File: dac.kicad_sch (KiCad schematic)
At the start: 53 parts, among them J9 DAC OUT, Q2 FMMT591, Q3 FMMT491, Q4 FMMT491, Q5 FMMT591, U1 CJC4334H, U9 OPA1612AxD

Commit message: Fixed VA/2
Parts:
- removed R52, R53: 10kΩ, PCM_JLCPCB:R_0805, symbol PCM_JLCPCB-Resistors:0805,10kΩ
- added R52, R53: 2.2kΩ, PCM_JLCPCB:R_0805, symbol PCM_JLCPCB-Resistors:0805,2.2kΩ
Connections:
- net GNDA: now also R52.1
- net VAO: now also R53.2
- net VA/2: now also R52.2, R53.1

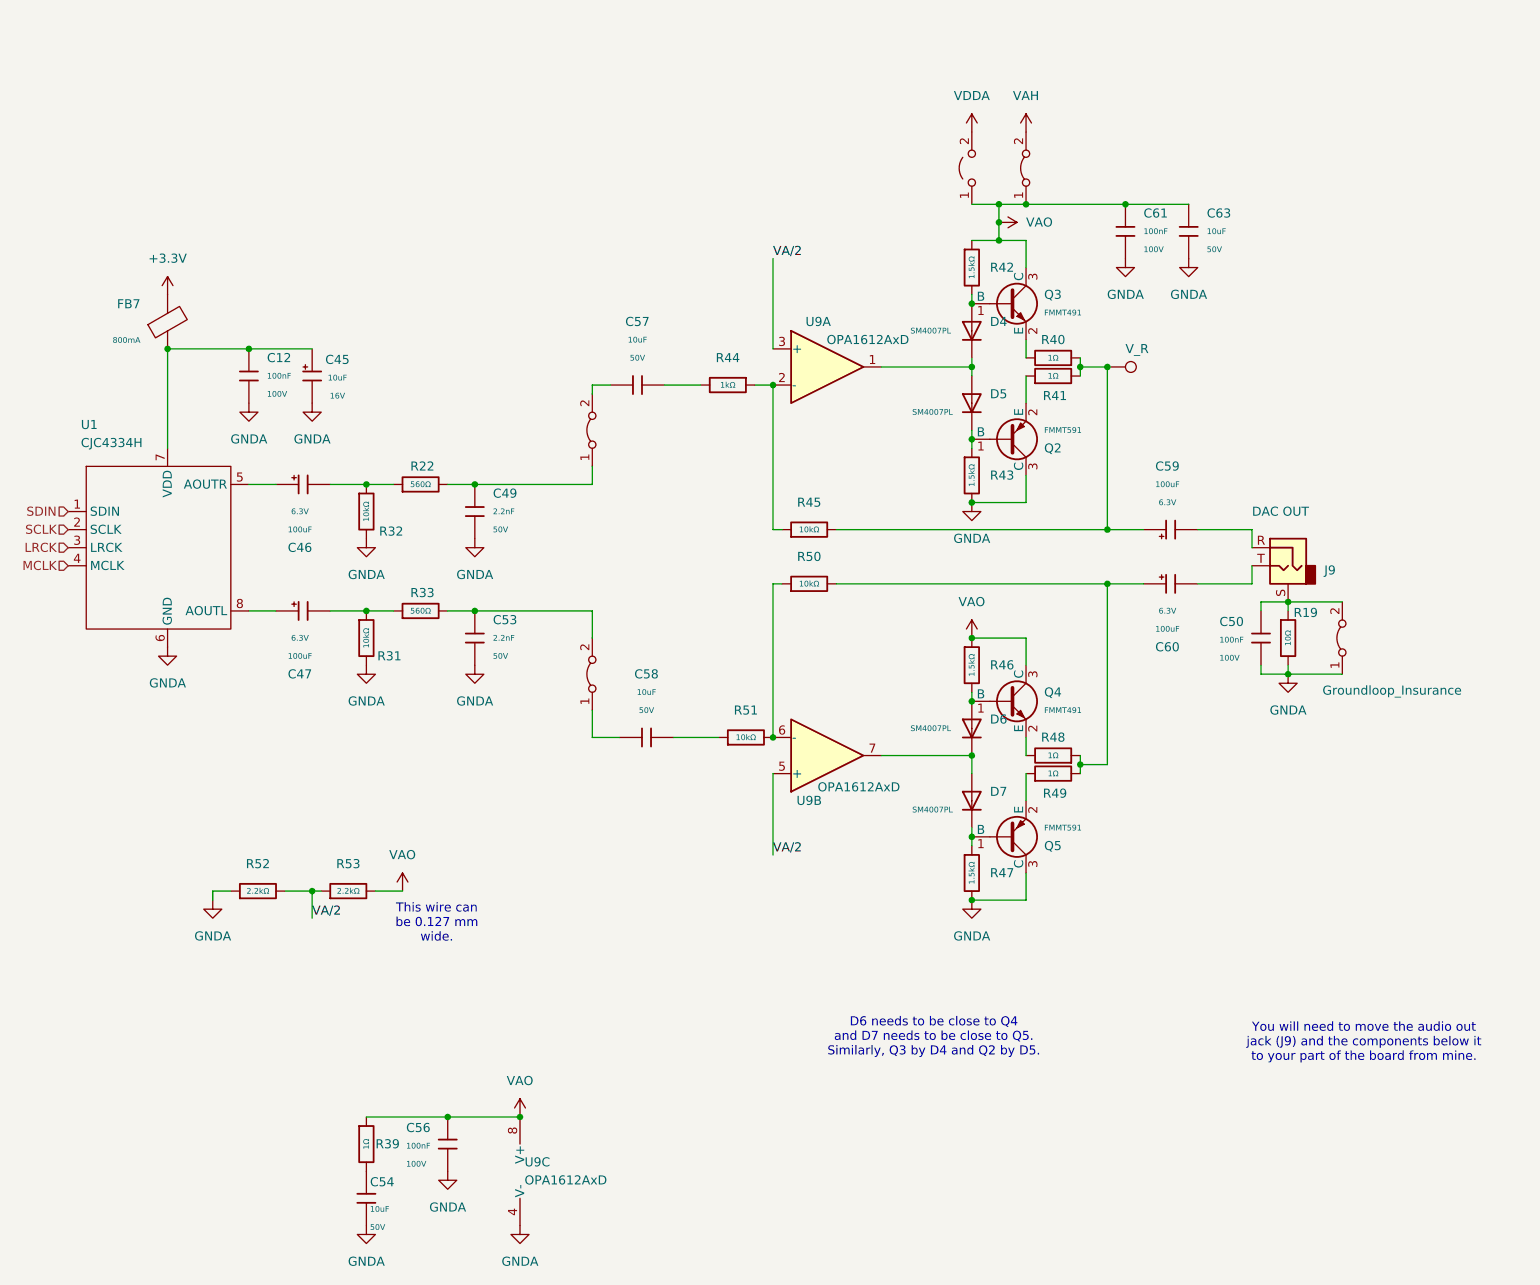
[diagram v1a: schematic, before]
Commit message: Changes from simulations.
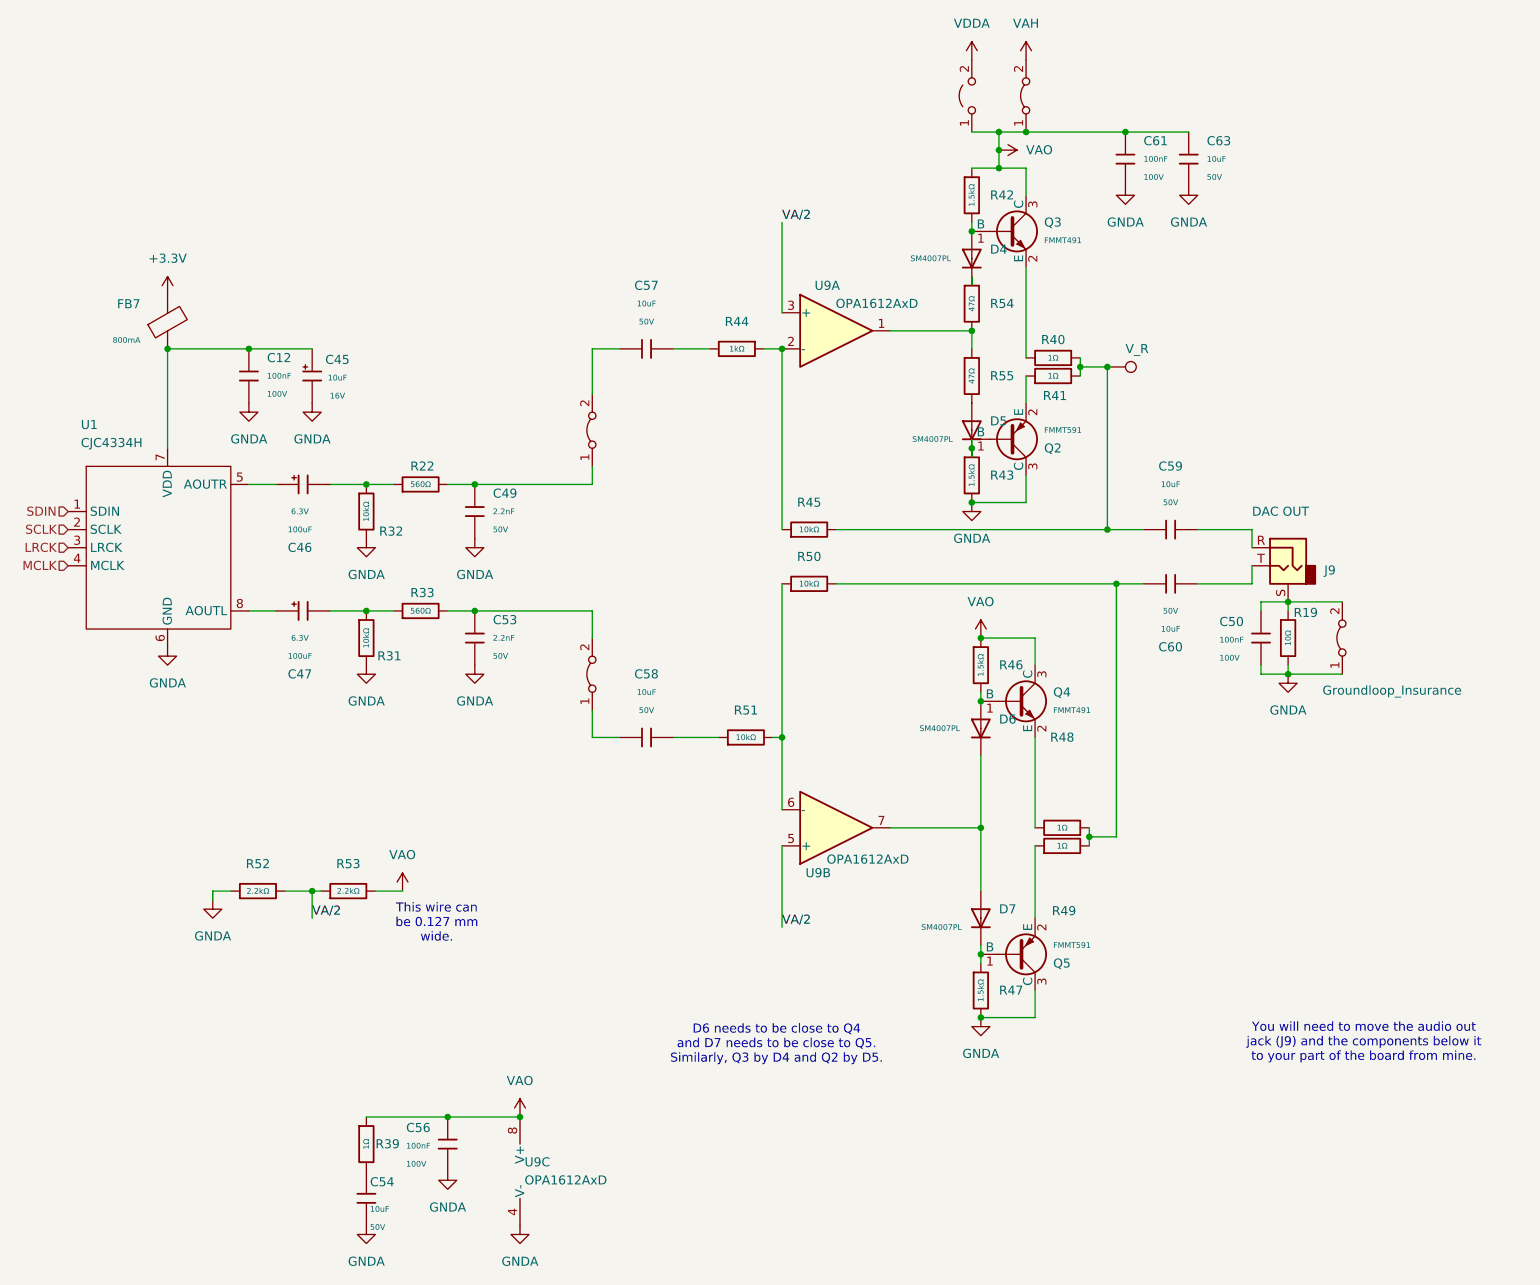
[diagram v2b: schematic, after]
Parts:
- removed C59, C60: 100uF, PCM_JLCPCB:C_CASE-B-3528-21(mm), symbol PCM_JLCPCB-Capacitors:CASE-B-3528-21(mm),100uF
- added C59, C60: 10uF, PCM_JLCPCB:C_0805, symbol PCM_JLCPCB-Capacitors:0805,10uF,(2)
- added R54, R55: 47Ω, PCM_JLCPCB:R_0805, symbol PCM_JLCPCB-Resistors:0805,47Ω
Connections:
- net at R48.1, R49.2, R50.2: now also C60.1
- net at J9.T: now also C60.2
- net at J9.R: now also C59.2
- net at R40.1, R41.2, R45.2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: now also C59.1
- new net: D4.1, R54.1
- new net: R54.2, R55.1, U9.1
- new net: D5.2, R55.2
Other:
- moved on the sheet: C57, C61, C63, D4, D5, D6, D7, Q3, Q4, Q5, R42, R44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

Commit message: Forgot the other channel.
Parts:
- removed R54, R55: 47Ω, PCM_JLCPCB:R_0805, symbol PCM_JLCPCB-Resistors:0805,47Ω
- added R54, R55, R56, R57: 100Ω, PCM_JLCPCB:R_0805, symbol PCM_JLCPCB-Resistors:0805,100Ω
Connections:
- net at D4.1: now also R55.1
- net at U9.1: now also R54.1, R55.2
- net at D5.2: now also R54.2
- new net: R56.2, R57.1, U9.7
- new net: D7.2, R57.2
- new net: D6.1, R56.1
